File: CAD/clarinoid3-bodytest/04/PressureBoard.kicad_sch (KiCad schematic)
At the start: 3 parts, among them J1 header i2c pressure, U1 Pressure1_0x28_I2C0

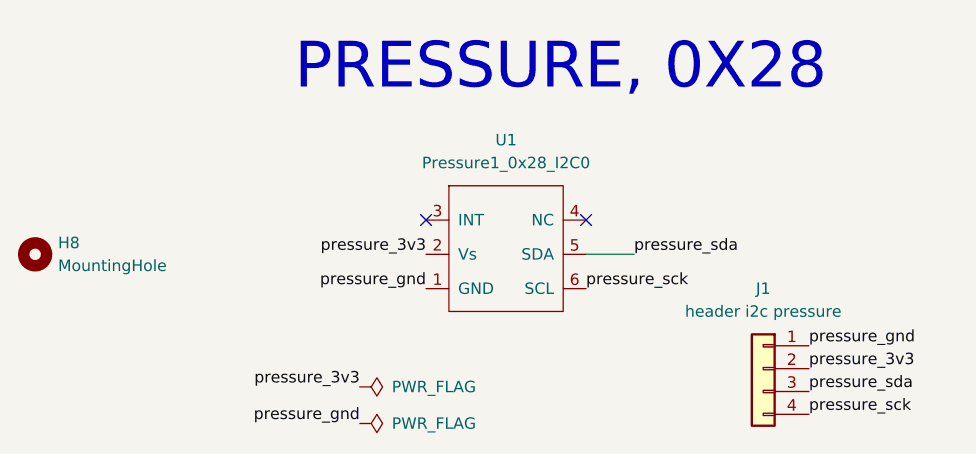
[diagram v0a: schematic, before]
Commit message: c3 design work adding more 3dp tests
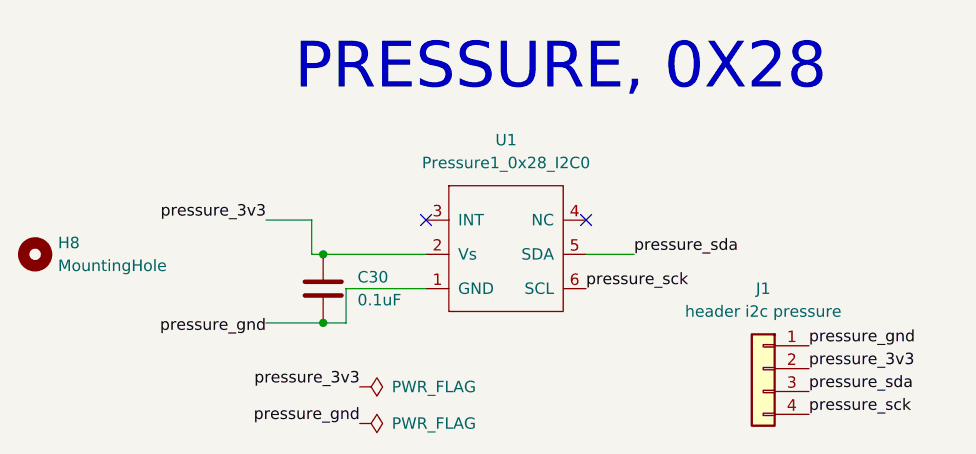
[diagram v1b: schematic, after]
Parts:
- added C30: 0.1uF, Capacitor_SMD:C_0603_1608Metric, symbol Device:C
- U1: footprint SamacSys_Parts:ABPMAND001PG2A3 -> clarinoid2:Honeywell-ABPMAND001PG2A3
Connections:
- net pressure_3v3: now also C30.1
- net pressure_gnd: no longer U1.1 (GND)
- new net: C30.2, U1.1 (GND)
